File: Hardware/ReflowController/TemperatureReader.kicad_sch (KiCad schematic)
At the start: 12 parts, among them U4 MAX31865xAP

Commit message: finished the io control for the pcb, need to define what is the best way for a remote keypad
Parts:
- renumbered D2 to D1, D1 to D2, NT3 to NT32, NT2 to NT33, R3 to R2, R1 to R3, R2 to R4
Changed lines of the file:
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@@
   (symbol (lib_id "Device:R") (at 144.78 85.09 0) (unit 1)
     (in_bom yes) (on_board yes) (dnp no) (fields_autoplaced)
-    (property "Reference" "R1" (at 147.32 84.455 0)
+    (property "Reference" "R3" (at 147.32 84.455 0)
       (effects (font (size 1.27 1.27)) (justify left))
     )
@@
       (project "ReflowController"
         (path "/2394cc2a-b9b0-4c0b-be11-1fc6085b0d5c/cedd135a-27b6-4ce6-9f5e-bdcd93291ccf"
-          (reference "R1") (unit 1)
+          (reference "R3") (unit 1)
         )
       )
@@
   (symbol (lib_id "Device:D_Zener") (at 195.58 120.65 270) (unit 1)
     (in_bom yes) (on_board yes) (dnp no) (fields_autoplaced)
-    (property "Reference" "D1" (at 198.12 120.015 90)
+    (property "Reference" "D2" (at 198.12 120.015 90)
       (effects (font (size 1.27 1.27)) (justify left))
     )
@@
       (project "ReflowController"
         (path "/2394cc2a-b9b0-4c0b-be11-1fc6085b0d5c/cedd135a-27b6-4ce6-9f5e-bdcd93291ccf"
-          (reference "D1") (unit 1)
+          (reference "D2") (unit 1)
         )
       )
@@
   (symbol (lib_id "Device:R") (at 154.94 85.09 0) (unit 1)
     (in_bom yes) (on_board yes) (dnp no) (fields_autoplaced)
-    (property "Reference" "R2" (at 157.48 84.455 0)
+    (property "Reference" "R4" (at 157.48 84.455 0)
       (effects (font (size 1.27 1.27)) (justify left))
     )
@@
       (project "ReflowController"
         (path "/2394cc2a-b9b0-4c0b-be11-1fc6085b0d5c/cedd135a-27b6-4ce6-9f5e-bdcd93291ccf"
-          (reference "R2") (unit 1)
+          (reference "R4") (unit 1)
         )
       )
@@
   (symbol (lib_id "Device:NetTie_2") (at 119.38 57.15 90) (unit 1)
     (in_bom no) (on_board yes) (dnp no) (fields_autoplaced)
-    (property "Reference" "NT3" (at 120.65 56.515 90)
+    (property "Reference" "NT32" (at 120.65 56.515 90)
       (effects (font (size 1.27 1.27)) (justify right))
     )
@@
       (project "ReflowController"
         (path "/2394cc2a-b9b0-4c0b-be11-1fc6085b0d5c/cedd135a-27b6-4ce6-9f5e-bdcd93291ccf"
-          (reference "NT3") (unit 1)
+          (reference "NT32") (unit 1)
         )
       )
@@
   (symbol (lib_id "Device:D_Zener") (at 180.34 120.65 270) (unit 1)
     (in_bom yes) (on_board yes) (dnp no) (fields_autoplaced)
-    (property "Reference" "D2" (at 182.88 120.015 90)
+    (property "Reference" "D1" (at 182.88 120.015 90)
       (effects (font (size 1.27 1.27)) (justify left))
     )
@@
       (project "ReflowController"
         (path "/2394cc2a-b9b0-4c0b-be11-1fc6085b0d5c/cedd135a-27b6-4ce6-9f5e-bdcd93291ccf"
-          (reference "D2") (unit 1)
+          (reference "D1") (unit 1)
         )
       )
@@
   (symbol (lib_id "Device:NetTie_2") (at 119.38 122.682 90) (unit 1)
     (in_bom no) (on_board yes) (dnp no) (fields_autoplaced)
-    (property "Reference" "NT2" (at 120.65 122.047 90)
+    (property "Reference" "NT33" (at 120.65 122.047 90)
       (effects (font (size 1.27 1.27)) (justify right))
     )
@@
       (project "ReflowController"
         (path "/2394cc2a-b9b0-4c0b-be11-1fc6085b0d5c/cedd135a-27b6-4ce6-9f5e-bdcd93291ccf"
-          (reference "NT2") (unit 1)
+          (reference "NT33") (unit 1)
         )
       )
@@
   (symbol (lib_id "Device:R") (at 82.55 72.39 0) (unit 1)
     (in_bom yes) (on_board yes) (dnp no) (fields_autoplaced)
-    (property "Reference" "R3" (at 85.09 71.755 0)
+    (property "Reference" "R2" (at 85.09 71.755 0)
       (effects (font (size 1.27 1.27)) (justify left))
     )
@@
       (project "ReflowController"
         (path "/2394cc2a-b9b0-4c0b-be11-1fc6085b0d5c/cedd135a-27b6-4ce6-9f5e-bdcd93291ccf"
-          (reference "R3") (unit 1)
-        )
-      )
+          (reference "R2") (unit 1)
+        )
+      )

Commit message: Wrking with edwin on the hwole schematic
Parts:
- removed C1, C2: 100n, Capacitor_SMD:C_1206_3216Metric, symbol Device:C
- removed R2: 10k, Resistor_SMD:R_1206_3216Metric, symbol Device:R
- removed R4: 10M, Resistor_SMD:R_1206_3216Metric, symbol Device:R
- added C4 (x2): 0.1uF, Capacitor_SMD:C_1206_3216Metric, symbol Device:C
- added R24: 10M, Resistor_SMD:R_0603_1608Metric_Pad0.98x0.95mm_HandSolder, symbol Device:R
- added R24: 10k, Resistor_SMD:R_0603_1608Metric_Pad0.98x0.95mm_HandSolder, symbol Device:R
- C3: Field8 (none) -> 490-1754-2-ND; disti (none) -> digikey; man (none) -> murata; man_no (none) -> GRM3195C1H103JA01D
- D1, D2, D3: footprint (none) -> Diode_SMD:D_SMB_Handsoldering; disti (none) -> digikey; disti_no (none) -> 497-2496-2-ND; man (none) -> stm; man_no (none) -> SMLVT3V3
- R3: footprint (none) -> Resistor_SMD:R_1206_3216Metric; disti (none) -> digikey; disti_no (none) -> A140365TR-ND; man (none) -> te; manNo RQ73C2B402RBTD -> (none); man_no (none) -> RQ73C2B402RBTD
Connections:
- net +3.3VD: now also C4.2, R24.2
- net DGND: now also C4.1
- net PT100_+IN: now also R24.1
- net REFIN+: now also R24.2
- net T_AGND: now also C4.2
- net ~{CS}: now also R24.1
- net at NT32.1, U4.3 (VDD): now also C4.1

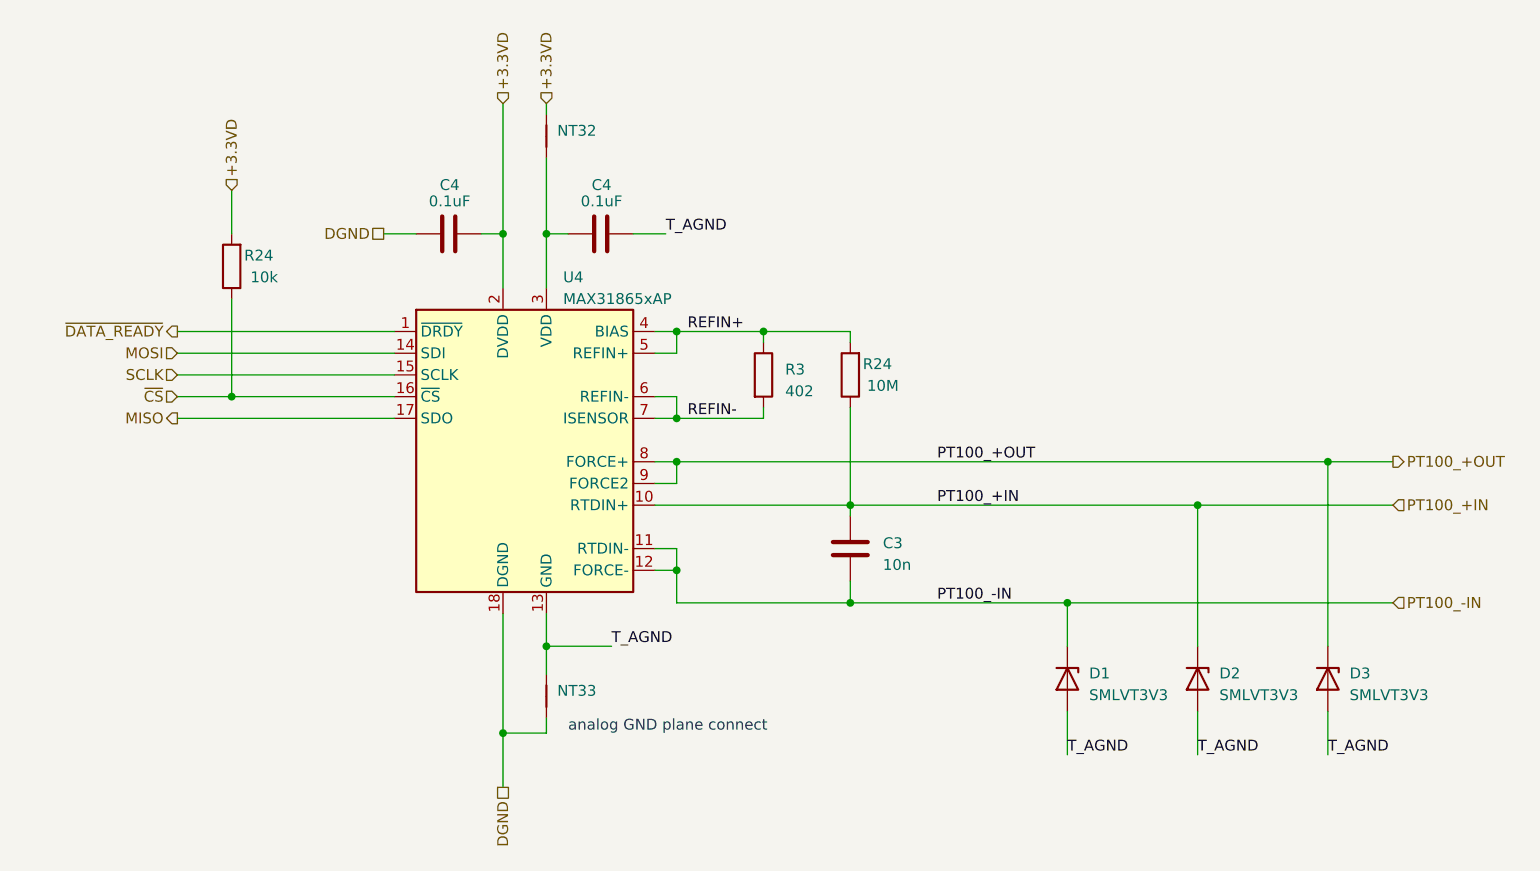
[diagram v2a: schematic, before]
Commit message: Finished the desing of the PSUand started with the PCB TODO: missing fuse find a solution
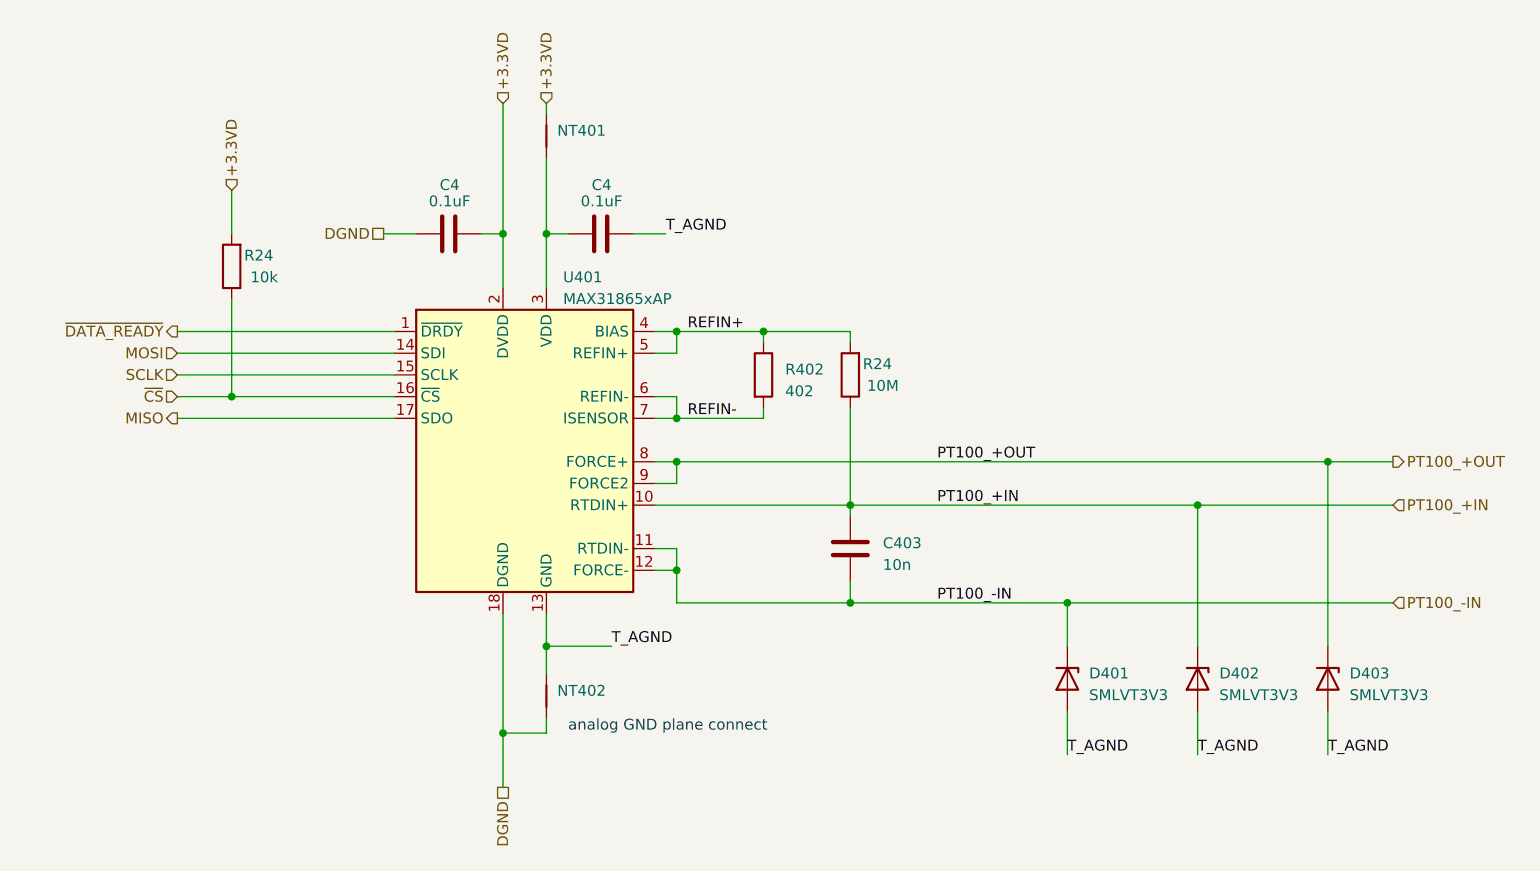
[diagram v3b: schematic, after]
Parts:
- NT401: renamed from NT32; footprint (none) -> NetTie:NetTie-2_SMD_Pad0.5mm
- NT402: renamed from NT33; footprint (none) -> NetTie:NetTie-2_SMD_Pad0.5mm
- renumbered C3 to C403, D1 to D401, D2 to D402, D3 to D403, R3 to R402, U4 to U401
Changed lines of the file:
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@@
   (symbol (lib_id "Sensor_Temperature:MAX31865xAP") (at 116.84 95.25 0) (unit 1)
     (in_bom yes) (on_board yes) (dnp no) (fields_autoplaced)
-    (property "Reference" "U4" (at 121.3359 73.66 0)
+    (property "Reference" "U401" (at 121.3359 73.66 0)
       (effects (font (size 1.27 1.27)) (justify left))
     )
@@
       (project "ReflowController"
         (path "/2394cc2a-b9b0-4c0b-be11-1fc6085b0d5c/cedd135a-27b6-4ce6-9f5e-bdcd93291ccf"
-          (reference "U4") (unit 1)
+          (reference "U401") (unit 1)
         )
       )
@@
   (symbol (lib_id "Device:C") (at 154.94 105.41 180) (unit 1)
     (in_bom yes) (on_board yes) (dnp no) (fields_autoplaced)
-    (property "Reference" "C3" (at 158.75 104.775 0)
+    (property "Reference" "C403" (at 158.75 104.775 0)
       (effects (font (size 1.27 1.27)) (justify right))
     )
@@
       (project "ReflowController"
         (path "/2394cc2a-b9b0-4c0b-be11-1fc6085b0d5c/cedd135a-27b6-4ce6-9f5e-bdcd93291ccf"
-          (reference "C3") (unit 1)
+          (reference "C403") (unit 1)
         )
       )
@@
   (symbol (lib_id "Device:D_Zener") (at 195.58 120.65 270) (unit 1)
     (in_bom yes) (on_board yes) (dnp no) (fields_autoplaced)
-    (property "Reference" "D2" (at 198.12 120.015 90)
+    (property "Reference" "D402" (at 198.12 120.015 90)
       (effects (font (size 1.27 1.27)) (justify left))
     )
@@
       (project "ReflowController"
         (path "/2394cc2a-b9b0-4c0b-be11-1fc6085b0d5c/cedd135a-27b6-4ce6-9f5e-bdcd93291ccf"
-          (reference "D2") (unit 1)
+          (reference "D402") (unit 1)
         )
       )
@@
   (symbol (lib_id "Device:R") (at 144.78 85.09 0) (unit 1)
     (in_bom yes) (on_board yes) (dnp no) (fields_autoplaced)
-    (property "Reference" "R3" (at 147.32 84.455 0)
+    (property "Reference" "R402" (at 147.32 84.455 0)
       (effects (font (size 1.27 1.27)) (justify left))
     )
@@
       (project "ReflowController"
         (path "/2394cc2a-b9b0-4c0b-be11-1fc6085b0d5c/cedd135a-27b6-4ce6-9f5e-bdcd93291ccf"
-          (reference "R3") (unit 1)
+          (reference "R402") (unit 1)
         )
       )
@@
         )
         (path "/2394cc2a-b9b0-4c0b-be11-1fc6085b0d5c/cedd135a-27b6-4ce6-9f5e-bdcd93291ccf"
-          (reference "R2") (unit 1)
+          (reference "R403") (unit 1)
         )
       )
@@
         )
         (path "/2394cc2a-b9b0-4c0b-be11-1fc6085b0d5c/cedd135a-27b6-4ce6-9f5e-bdcd93291ccf"
-          (reference "C1") (unit 1)
+          (reference "C401") (unit 1)
         )
       )
@@
   (symbol (lib_id "Device:NetTie_2") (at 119.38 57.15 90) (unit 1)
     (in_bom no) (on_board yes) (dnp no) (fields_autoplaced)
-    (property "Reference" "NT32" (at 120.65 56.515 90)
+    (property "Reference" "NT401" (at 120.65 56.515 90)
       (effects (font (size 1.27 1.27)) (justify right))
     )
@@
       (effects (font (size 1.27 1.27)) (justify right) hide)
     )
-    (property "Footprint" "" (at 119.38 57.15 0)
+    (property "Footprint" "NetTie:NetTie-2_SMD_Pad0.5mm" (at 119.38 57.15 0)
       (effects (font (size 1.27 1.27)) hide)
     )
@@
       (project "ReflowController"
         (path "/2394cc2a-b9b0-4c0b-be11-1fc6085b0d5c/cedd135a-27b6-4ce6-9f5e-bdcd93291ccf"
-          (reference "NT32") (unit 1)
+          (reference "NT401") (unit 1)
         )
       )
@@
         )
         (path "/2394cc2a-b9b0-4c0b-be11-1fc6085b0d5c/cedd135a-27b6-4ce6-9f5e-bdcd93291ccf"
-          (reference "R1") (unit 1)
+          (reference "R401") (unit 1)
         )
       )
@@
   (symbol (lib_id "Device:D_Zener") (at 180.34 120.65 270) (unit 1)
     (in_bom yes) (on_board yes) (dnp no) (fields_autoplaced)
-    (property "Reference" "D1" (at 182.88 120.015 90)
+    (property "Reference" "D401" (at 182.88 120.015 90)
       (effects (font (size 1.27 1.27)) (justify left))
     )
@@
       (project "ReflowController"
         (path "/2394cc2a-b9b0-4c0b-be11-1fc6085b0d5c/cedd135a-27b6-4ce6-9f5e-bdcd93291ccf"
-          (reference "D1") (unit 1)
+          (reference "D401") (unit 1)
         )
       )
@@
   (symbol (lib_id "Device:NetTie_2") (at 119.38 122.682 90) (unit 1)
     (in_bom no) (on_board yes) (dnp no) (fields_autoplaced)
-    (property "Reference" "NT33" (at 120.65 122.047 90)
+    (property "Reference" "NT402" (at 120.65 122.047 90)
       (effects (font (size 1.27 1.27)) (justify right))
     )
@@
       (effects (font (size 1.27 1.27)) (justify right) hide)
     )
-    (property "Footprint" "" (at 119.38 122.682 0)
+    (property "Footprint" "NetTie:NetTie-2_SMD_Pad0.5mm" (at 119.38 122.682 0)
       (effects (font (size 1.27 1.27)) hide)
     )
@@
       (project "ReflowController"
         (path "/2394cc2a-b9b0-4c0b-be11-1fc6085b0d5c/cedd135a-27b6-4ce6-9f5e-bdcd93291ccf"
-          (reference "NT33") (unit 1)
+          (reference "NT402") (unit 1)
         )
       )
@@
         )
         (path "/2394cc2a-b9b0-4c0b-be11-1fc6085b0d5c/cedd135a-27b6-4ce6-9f5e-bdcd93291ccf"
-          (reference "C2") (unit 1)
+          (reference "C402") (unit 1)
         )
       )
@@
   (symbol (lib_id "Device:D_Zener") (at 210.82 120.65 270) (unit 1)
     (in_bom yes) (on_board yes) (dnp no) (fields_autoplaced)
-    (property "Reference" "D3" (at 213.36 120.015 90)
+    (property "Reference" "D403" (at 213.36 120.015 90)
       (effects (font (size 1.27 1.27)) (justify left))
     )
@@
       (project "ReflowController"
         (path "/2394cc2a-b9b0-4c0b-be11-1fc6085b0d5c/cedd135a-27b6-4ce6-9f5e-bdcd93291ccf"
-          (reference "D3") (unit 1)
-        )
-      )
+          (reference "D403") (unit 1)
+        )
+      )
